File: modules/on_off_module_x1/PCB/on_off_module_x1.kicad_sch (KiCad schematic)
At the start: 25 parts, among them J1 Screw_Terminal_01x02, J2 Conn_01x06_Socket, J3 Conn_01x03_Socket, J4 Screw_Terminal_01x02, J5 Screw_Terminal_01x02, K1 12V 5A, Q1 2N7002H, SW1 SW_SPDT, U1 AMS1117-3.3, U2 ESP-12E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

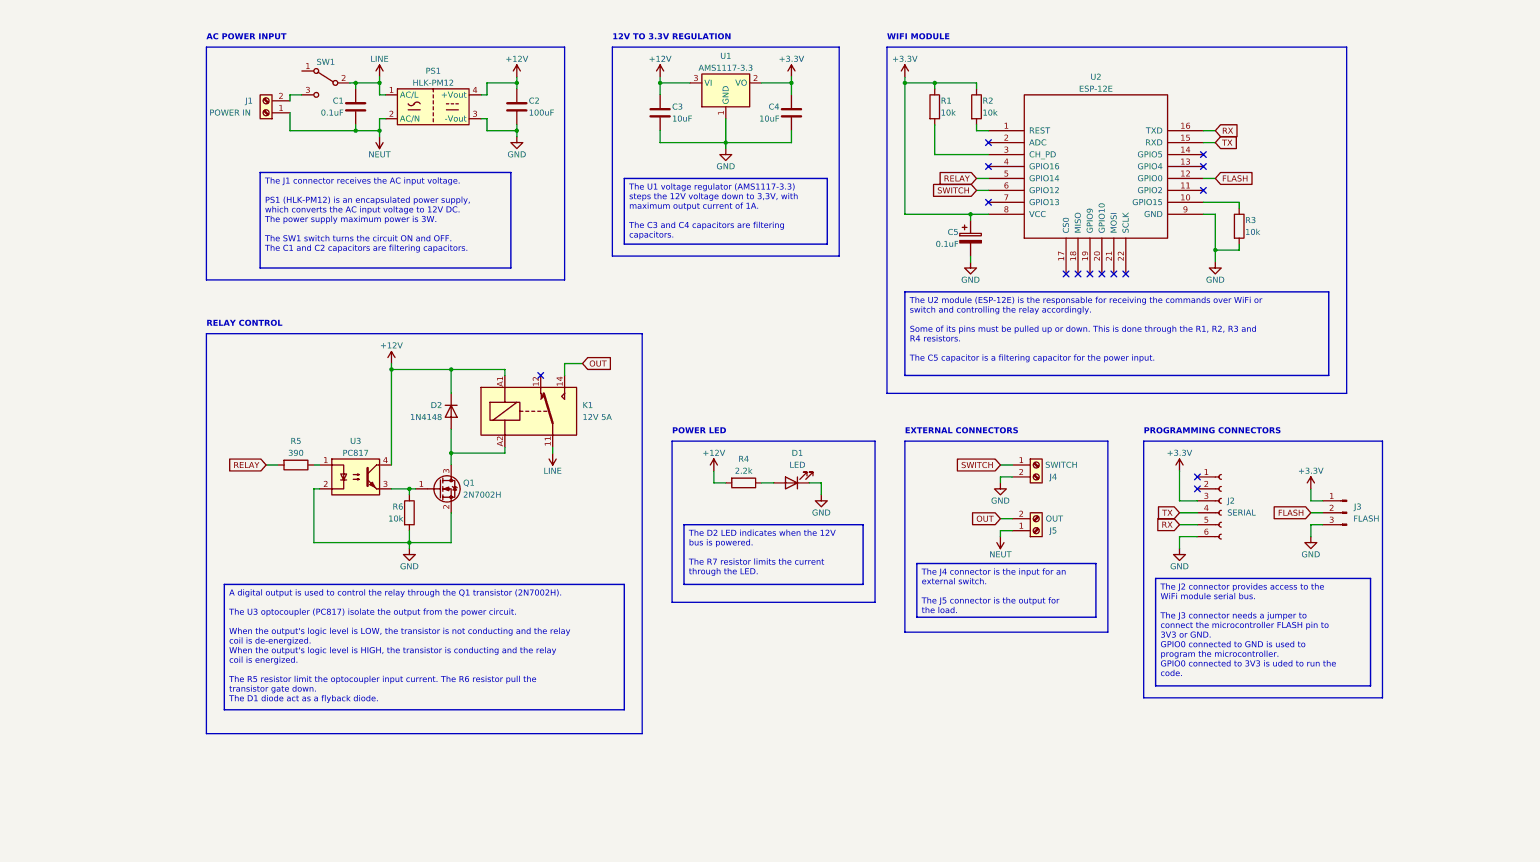
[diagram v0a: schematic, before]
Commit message: ON-OFF module hardware updated to V2
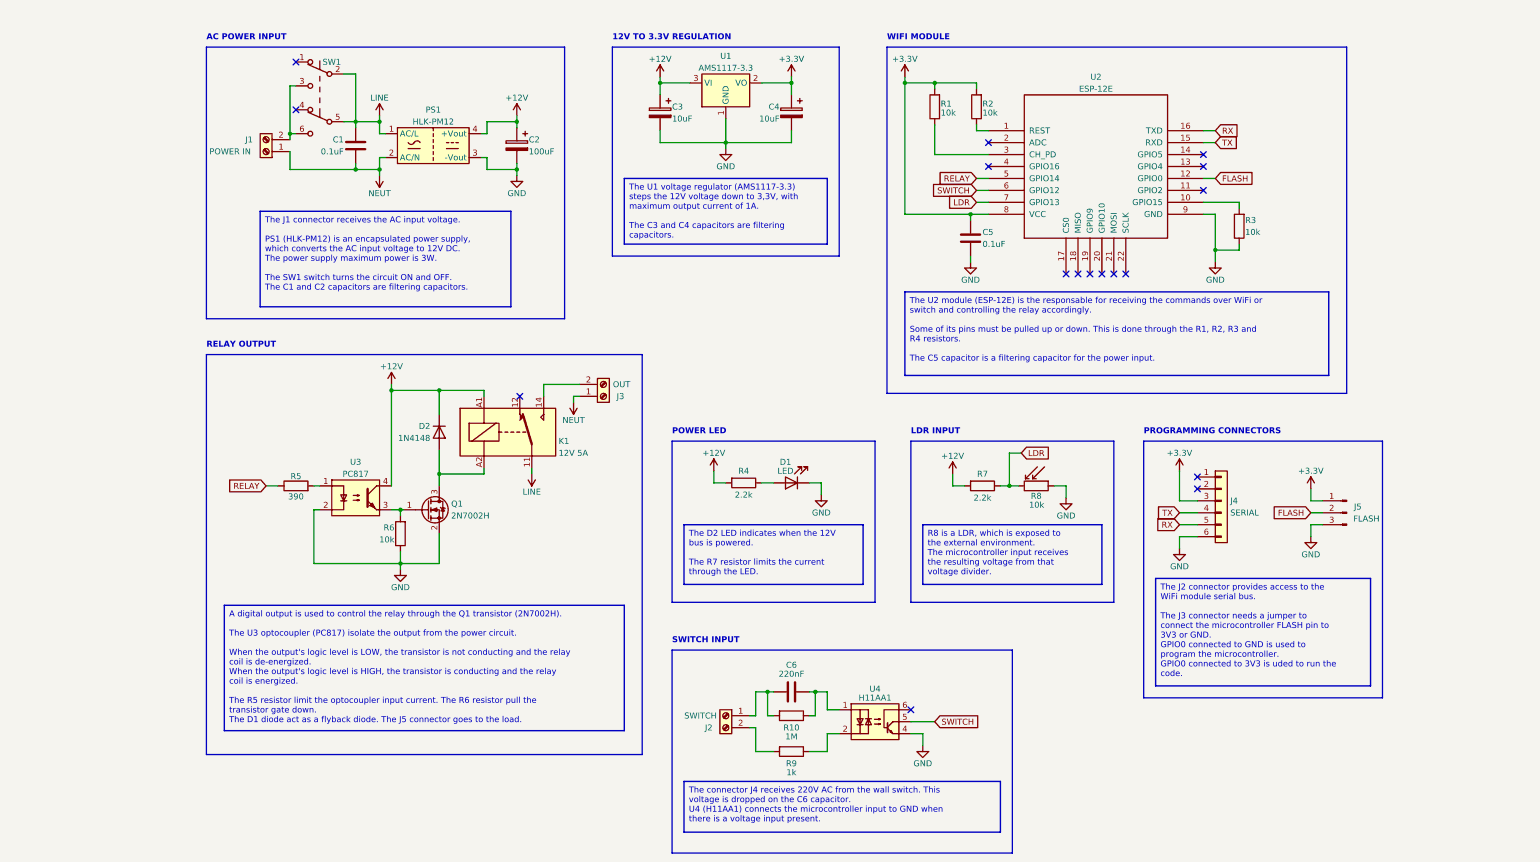
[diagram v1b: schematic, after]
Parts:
- added C6: 220nF, Alan_Capacitor:CAP_THT_CERAMIC_X2_13x6x12, symbol Alan_Capacitor:CAP_THT_CERAMIC_X2_13x6x12
- added R10: 1M, Alan_Resistor:RES_SMD_1206, symbol Alan_Resistor:RES_SMD_1206
- added R7: 2.2k, Alan_Resistor:RES_SMD_0603, symbol Alan_Resistor:RES_SMD_0603
- added R8: 10k, Alan_Sensor:LDR_5_V, symbol Alan_Sensor:LDR_THT_5mm
- added R9: 1k, Alan_Resistor:RES_SMD_1206, symbol Alan_Resistor:RES_SMD_1206
- added U4: H11AA1, Alan_IC:SMDIP-6_7.62, symbol Alan_IC:H11AA1
- C1: footprint Capacitor_THT:C_Rect_L18.0mm_W6.0mm_P15.00mm_FKS3_FKP3 -> Alan_Capacitor:CAP_THT_CERAMIC_X2_18x6x15; symbol Device:C -> Alan_Capacitor:CAP_THT_CERAMIC_X2_18x6x15
- C2: footprint Capacitor_SMD:CP_Elec_6.3x7.7 -> Alan_Capacitor:CAP_SMD_ELEC_6.3x7.7; symbol Device:C -> Alan_Capacitor:CAP_SMD_ELEC_6.3x7.7
- C3, C4: footprint Capacitor_Tantalum_SMD:CP_EIA-3216-18_Kemet-A -> Alan_Capacitor:CAP_SMD_TANTALUM_CASE-A; symbol Device:C -> Alan_Capacitor:CAP_SMD_TANTALUM_CASE-A
- C5: footprint Capacitor_SMD:C_0603_1608Metric -> Alan_Capacitor:CAP_SMD_CERAMIC_0603; symbol Device:C_Polarized -> Alan_Capacitor:CAP_SMD_CERAMIC_0603
- D1: footprint LED_SMD:LED_0603_1608Metric -> Alan_LED:LED_SMD_0603; symbol Device:LED -> Alan_LED:LED_SMD_0603
- D2: footprint Diode_SMD:D_SOD-323F -> Alan_Diode:DIODE_SMD_SOD323F; symbol Diode:1N4148 -> Alan_Diode:DIODE_1N4148
- J1: footprint TerminalBlock_Phoenix:TerminalBlock_Phoenix_MKDS-1,5-2-5.08_1x02_P5.08mm_Horizontal -> Alan_Connector:CONN_TERMINAL-BLOCK_2P_P5.08; symbol Connector:Screw_Terminal_01x02 -> Alan_Connector:CONN_TERMINAL-BLOCK_2P_P5.08
- J2: renamed from J4; footprint TerminalBlock_Phoenix:TerminalBlock_Phoenix_MKDS-1,5-2-5.08_1x02_P5.08mm_Horizontal -> Alan_Connector:CONN_TERMINAL-BLOCK_2P_P5.08; symbol Connector:Screw_Terminal_01x02 -> Alan_Connector:CONN_TERMINAL-BLOCK_2P_P5.08
- J3: renamed from J5; footprint TerminalBlock_Phoenix:TerminalBlock_Phoenix_MKDS-1,5-2-5.08_1x02_P5.08mm_Horizontal -> Alan_Connector:CONN_TERMINAL-BLOCK_2P_P5.08; symbol Connector:Screw_Terminal_01x02 -> Alan_Connector:CONN_TERMINAL-BLOCK_2P_P5.08
- J4: renamed from J2; footprint Connector_PinHeader_2.54mm:PinHeader_1x06_P2.54mm_Vertical -> Alan_Connector:CONN_SOCKET-HEADER_1x06_V; symbol Connector:Conn_01x06_Socket -> Alan_Connector:CONN_SOCKET-HEADER_1x06_V
- J5: renamed from J3; footprint Connector_PinSocket_2.54mm:PinSocket_1x03_P2.54mm_Vertical -> Alan_Connector:CONN_PIN-HEADER_1x03_V
- K1: footprint Relay_THT:Relay_SPDT_Finder_36.11 -> Alan_Relay:RELAY_SPDT_FINDER_36.11; symbol Relay:FINDER-36.11 -> Alan_Relay:RELAY_SPDT_FINDER-36.11
- PS1: footprint Converter_ACDC:Converter_ACDC_HiLink_HLK-PMxx -> Alan_Module:HILINK_HLK-PMxx; symbol Converter_ACDC:HLK-PM12 -> Alan_Module:MOD_HILINK_HLK-PM12
- Q1: footprint Package_TO_SOT_SMD:SOT-23 -> Alan_Transistor:SOT-23; symbol Transistor_FET:2N7002H -> Alan_Transistor:MOSFET_SMD_2N7002H
- R1, R2, R3, R4, R5, R6: footprint Resistor_SMD:R_0603_1608Metric -> Alan_Resistor:RES_SMD_0603; symbol Device:R -> Alan_Resistor:RES_SMD_0603
- SW1: footprint MyLibrary:Toggle_Switch_SelfLocking_7x7 -> Alan_Switches:SW_TOGGLE_DPDT_THT_7x7; symbol Switch:SW_SPDT -> Alan_Switches:SW_TOGGLE_DPDT_THT_7x7
- U1: footprint Package_TO_SOT_SMD:SOT-223-3_TabPin2 -> Alan_IC:SOT-223-3_TAB2; symbol Regulator_Linear:AMS1117-3.3 -> Alan_IC:AMS1117-3.3
- U2: footprint ESP8266:ESP-12E_SMD -> Alan_Module:MOD_ESP-12E; symbol ESP8266:ESP-12E -> Alan_Module:MOD_ESP-12E
- U3: footprint Package_DIP:SMDIP-4_W7.62mm -> Alan_IC:SMDIP-4_7.62; symbol Isolator:PC817 -> Alan_IC:PC817
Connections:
- net +12V: now also R4.1, R7.1; no longer R4.2
- net +3.3V: now also C5.2; no longer C5.1
- net GND: now also C5.1, R8.1, U4.4; no longer C5.2, J2.2 (Pin_2)
- net LINE: now also SW1.5 (B)
- net SWITCH: now also U4.5; no longer J2.1 (Pin_1)
- net at J1.2 (Pin_2), SW1.3 (C): now also SW1.6 (C)
- net at D1.2 (A): now also R4.2; no longer R4.1
- net LDR: now reaches U2.7 (GPIO13)
- net LDR: now also R7.2, R8.2
- net OUT: no longer names the net of J3.2 (Pin_2), K1.14
- new net: C6.1, J2.1 (Pin_1), R10.1
- new net: C6.2, R10.2, U4.1
- new net: J2.2 (Pin_2), R9.1
- new net: R9.2, U4.2
- no-connect marks 15 -> 17
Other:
- note added: "LDR INPUT"
- note added: "RELAY OUTPUT"
- note added: "SWITCH INPUT"
- note removed: "EXTERNAL CONNECTORS"
- note removed: "RELAY CONTROL"
- moved on the sheet: C1, D1, D2, J1, J2, J3, K1, PS1, Q1, R1, R2, R3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

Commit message: General files structure refactoring
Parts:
- removed D2: 1N4148, Alan_Diode:DIODE_SMD_SOD323F, symbol Alan_Diode:DIODE_1N4148
- removed J1, J2, J3: Screw_Terminal_01x02, Alan_Connector:CONN_TERMINAL-BLOCK_2P_P5.08, symbol Alan_Connector:CONN_TERMINAL-BLOCK_2P_P5.08
- removed SW1: SW_SPDT, Alan_Switches:SW_TOGGLE_DPDT_THT_7x7, symbol Alan_Switches:SW_TOGGLE_DPDT_THT_7x7
- added C7: 100nF, Alan_Capacitor:CAP_SMD_CERAMIC_0603, symbol Alan_Capacitor:CAP_SMD_CERAMIC_0603
- added D2: S1A, Alan_Diode:DIODE_SMD_SMA, symbol Alan_Diode:DIODE_S1A
- added F1: 0,25A, Alan_Fuse:FUSEHOLDER_THT_5x20_CLIP, symbol Alan_Fuse:FUSEHOLDER_THT_5x20_CLIP
- added J1: CONN_TERMINAL-BLOCK_5P_P5.08, Alan_Connector:CONN_TERMINAL-BLOCK_5P_P5.08, symbol Alan_Connector:CONN_TERMINAL-BLOCK_5P_P5.08
- added L1: 600R, Alan_Inductor:BEAD_SMD_1206, symbol Alan_Inductor:BEAD_SMD_1206
- added R11: 33k, Alan_Resistor:RES_SMD_1206, symbol Alan_Resistor:RES_SMD_1206
- added R12: 10k, Alan_Resistor:RES_SMD_0603, symbol Alan_Resistor:RES_SMD_0603
- C6: value 220nF -> 47nF; footprint Alan_Capacitor:CAP_THT_CERAMIC_X2_13x6x12 -> Alan_Capacitor:CAP_THT_CERAMIC_X2_13x5x11_P10; symbol Alan_Capacitor:CAP_THT_CERAMIC_X2_13x6x12 -> Alan_Capacitor:CAP_THT_CERAMIC_X2_13x5x11_P10; Voltage (none) -> 350V
- R10: value 1M -> 33k; Power (none) -> 1/4W; Tolerance (none) -> 5%
- R4: value 2.2k -> 2k2
- R5: value 390 -> 390R
- R7: value 2.2k -> 33k
- R9: value 1k -> 470k; Power (none) -> 1/4; Tolerance (none) -> 5%
- renumbered J4 to J2, J5 to J3
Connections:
- net +12V: now also D2.1 (K); no longer R7.1
- net +3.3V: now also R7.1
- net GND: now also C7.2
- net LDR: now also U2.2 (ADC); no longer U2.7 (GPIO13)
- net LINE: now also F1.2
- net NEUT: now also R10.1, J1.2 (Pin_2)
- net SWITCH: now also C7.1, R12.2; no longer U4.5
- net at C6.1: now also R9.1, L1.2; no longer R10.1
- net at C6.2, U4.1: now also R9.2; no longer R10.2
- net LOAD: now reaches K1.14
- net LOAD: now also J1.5 (Pin_5)
- net at K1.A2, Q1.3 (D): now also D2.2 (A)
- net at U4.2: now also R11.2; no longer R9.2
- net RX renamed UART-
- net TX renamed UART+
- new net: F1.1, J1.1 (Pin_1)
- new net: R12.1, U4.5
- new net: R10.2, R11.1
- new net Earth: J1.3 (Pin_3)
- new net SW_IN: J1.4 (Pin_4), L1.1
- no-connect marks 17 -> 15
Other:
- note added: "3.3V REGULATOR"
- note added: "MICROCONTROLLER"
- note added: "POWER SUPPLY"
- note added: "TERMINAL BLOCKS"
- note removed: "12V TO 3.3V REGULATION"
- note removed: "AC POWER INPUT"
- note removed: "WIFI MODULE"
- moved on the sheet: C1, C2, C3, C4, C5, C6, D1, J2, J3, K1, PS1, Q1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
